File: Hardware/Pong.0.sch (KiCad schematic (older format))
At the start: 0 parts

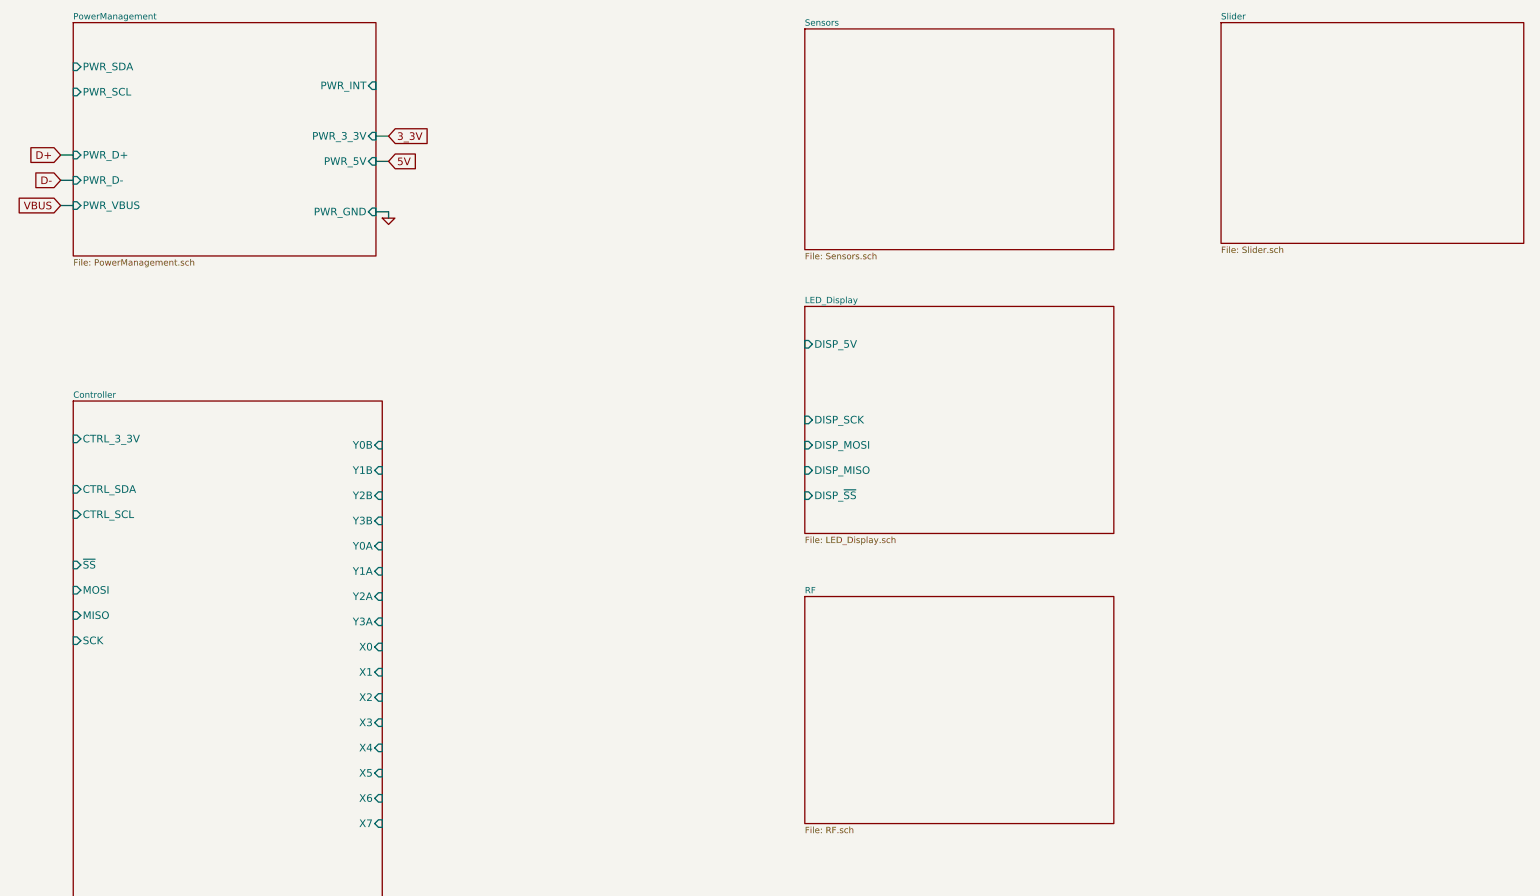
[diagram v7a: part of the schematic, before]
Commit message: Continued populating the schematics.
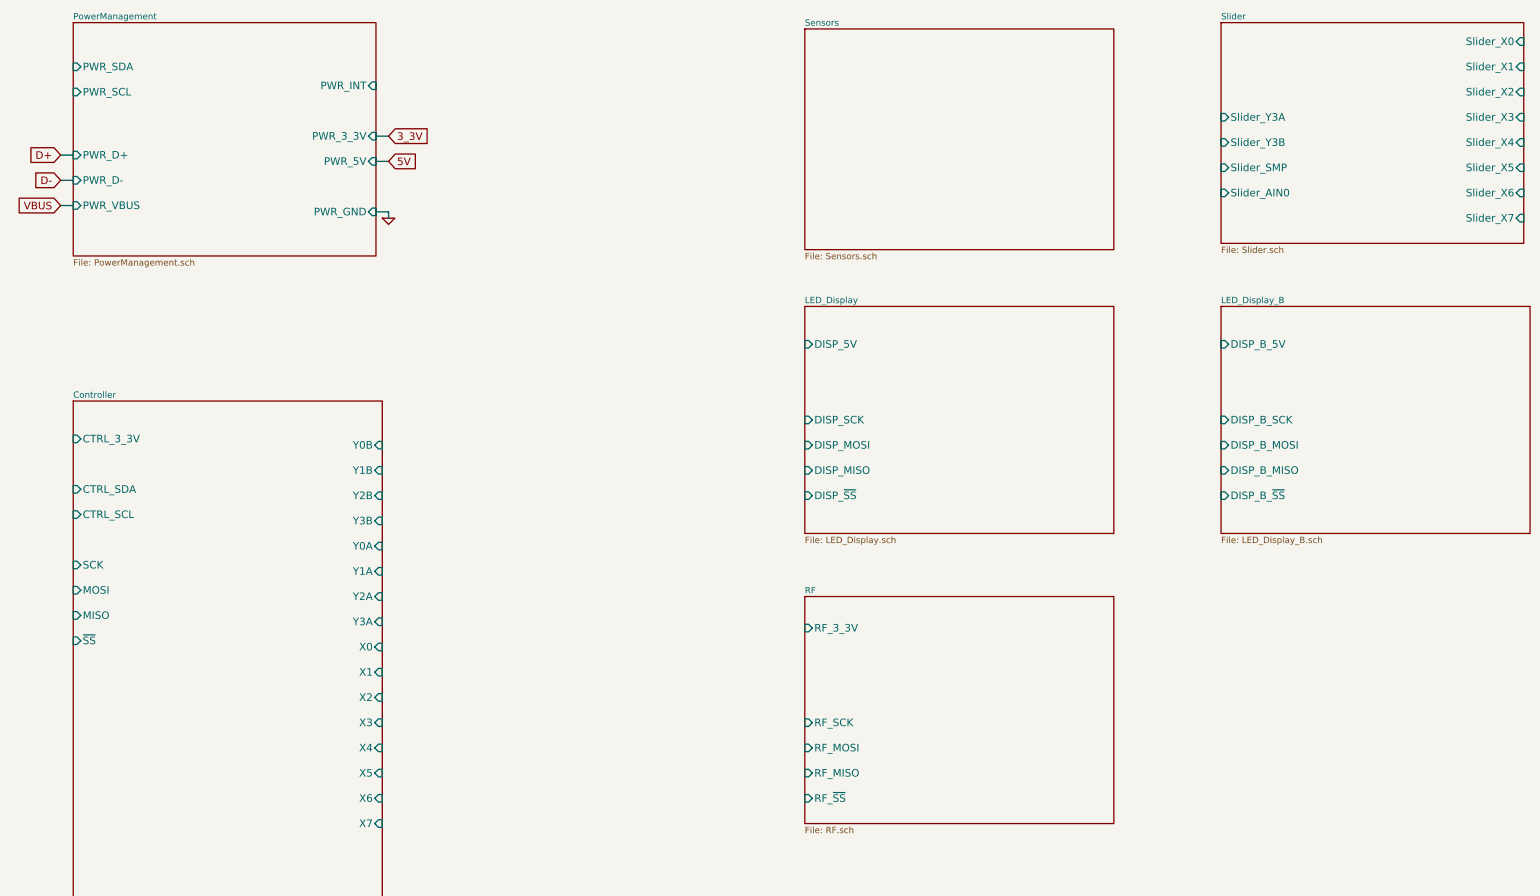
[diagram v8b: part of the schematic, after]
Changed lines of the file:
@@
 $Descr B 17000 11000
 encoding utf-8
-Sheet 1 7
+Sheet 1 8
 Title "Pong.0"
-Date "12 sep 2013"
-Rev "0.2"
+Date "19 sep 2013"
+Rev "0.3"
 Comp "Projects and Stuff LLC"
 Comment1 ""
@@
 6E 56 52 49 51 4E 59 71 7E 65 C5 4D 0F AF 00 BF F6 21 9D BA 45 88 9C 00 16 00 C0 66 90 E0 00 00
 AC 42 3B 38 00 00 AB 90 E0 00 00 AC 42 82 03 00 B0 EA FF 00 E3 76 B5 A7 81 B6 BC 08 00 00 00 00
-49 45 4E 44 AE 42 60 82 DC $EndBitmap
+49 45 4E 44 AE 42 60 82 20 $EndBitmap
 EndData
 $EndBitmap
@@
 F0 "RF" 50
 F1 "RF.sch" 50
+F2 "RF_3_3V" I L 8450 6100 60
+F3 "RF_SCK" I L 8450 6850 60
+F4 "RF_MOSI" I L 8450 7050 60
+F5 "RF_MISO" I L 8450 7250 60
+F6 "RF_~SS" I L 8450 7450 60
 $EndSheet
 Wire Wire Line
@@
 F0 "Sensors" 50
 F1 "Sensors.sch" 50
-$EndSheet
-$Sheet
-S 2650 4300 2450 4150
-U 522DE5CB
-F0 "Controller" 50
-F1 "Controller.sch" 50
-F2 "CTRL_3_3V" I L 2650 4600 60
-F3 "CTRL_SDA" I L 2650 5000 60
-F4 "CTRL_SCL" I L 2650 5200 60
-F5 "Y0B" I R 5100 4650 60
-F6 "Y1B" I R 5100 4850 60
-F7 "Y2B" I R 5100 5050 60
-F8 "Y3B" I R 5100 5250 60
-F9 "Y0A" I R 5100 5450 60
-F10 "Y1A" I R 5100 5650 60
-F11 "Y2A" I R 5100 5850 60
-F12 "Y3A" I R 5100 6050 60
-F13 "X0" I R 5100 6250 60
-F14 "X1" I R 5100 6450 60
-F15 "X2" I R 5100 6650 60
-F16 "X3" I R 5100 6850 60
-F17 "X4" I R 5100 7050 60
-F18 "X5" I R 5100 7250 60
-F19 "X6" I R 5100 7450 60
-F20 "X7" I R 5100 7650 60
-F21 "~SS" I L 2650 5600 60
-F22 "MOSI" I L 2650 5800 60
-F23 "MISO" I L 2650 6000 60
-F24 "SCK" I L 2650 6200 60
 $EndSheet
 $Sheet
@@
 $EndBitmap
 $Sheet
+S 2650 4300 2450 4150
+U 522DE5CB
+F0 "Controller" 50
+F1 "Controller.sch" 50
+F2 "CTRL_3_3V" I L 2650 4600 60
+F3 "CTRL_SDA" I L 2650 5000 60
+F4 "CTRL_SCL" I L 2650 5200 60
+F5 "Y0B" I R 5100 4650 60
+F6 "Y1B" I R 5100 4850 60
+F7 "Y2B" I R 5100 5050 60
+F8 "Y3B" I R 5100 5250 60
+F9 "Y0A" I R 5100 5450 60
+F10 "Y1A" I R 5100 5650 60
+F11 "Y2A" I R 5100 5850 60
+F12 "Y3A" I R 5100 6050 60
+F13 "X0" I R 5100 6250 60
+F14 "X1" I R 5100 6450 60
+F15 "X2" I R 5100 6650 60
+F16 "X3" I R 5100 6850 60
+F17 "X4" I R 5100 7050 60
+F18 "X5" I R 5100 7250 60
+F19 "X6" I R 5100 7450 60
+F20 "X7" I R 5100 7650 60
+F21 "~SS" I L 2650 6200 60
+F22 "MOSI" I L 2650 5800 60
+F23 "MISO" I L 2650 6000 60
+F24 "SCK" I L 2650 5600 60
+$EndSheet
+$Sheet
 S 11750 1300 2400 1750
 U 5231F823
 F0 "Slider" 50
 F1 "Slider.sch" 50
+F2 "Slider_X0" I R 14150 1450 60
+F3 "Slider_X1" I R 14150 1650 60
+F4 "Slider_X2" I R 14150 1850 60
+F5 "Slider_X3" I R 14150 2050 60
+F6 "Slider_X4" I R 14150 2250 60
+F7 "Slider_X5" I R 14150 2450 60
+F8 "Slider_X6" I R 14150 2650 60
+F9 "Slider_X7" I R 14150 2850 60
+F10 "Slider_Y3A" I L 11750 2050 60
+F11 "Slider_Y3B" I L 11750 2250 60
+F12 "Slider_SMP" I L 11750 2450 60
+F13 "Slider_AIN0" I L 11750 2650 60
+$EndSheet
+$Sheet
+S 11750 3550 2450 1800
+U 523B2459
+F0 "LED_Display_B" 50
+F1 "LED_Display_B.sch" 50
+F2 "DISP_B_SCK" I L 11750 4450 60
+F3 "DISP_B_MOSI" I L 11750 4650 60
+F4 "DISP_B_MISO" I L 11750 4850 60
+F5 "DISP_B_~SS" I L 11750 5050 60
+F6 "DISP_B_5V" I L 11750 3850 60
 $EndSheet
 $EndSCHEMATC
